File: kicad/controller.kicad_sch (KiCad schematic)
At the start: 18 parts, among them J9 SWD, SW6 RESET, U6 Pico, U7 TL431

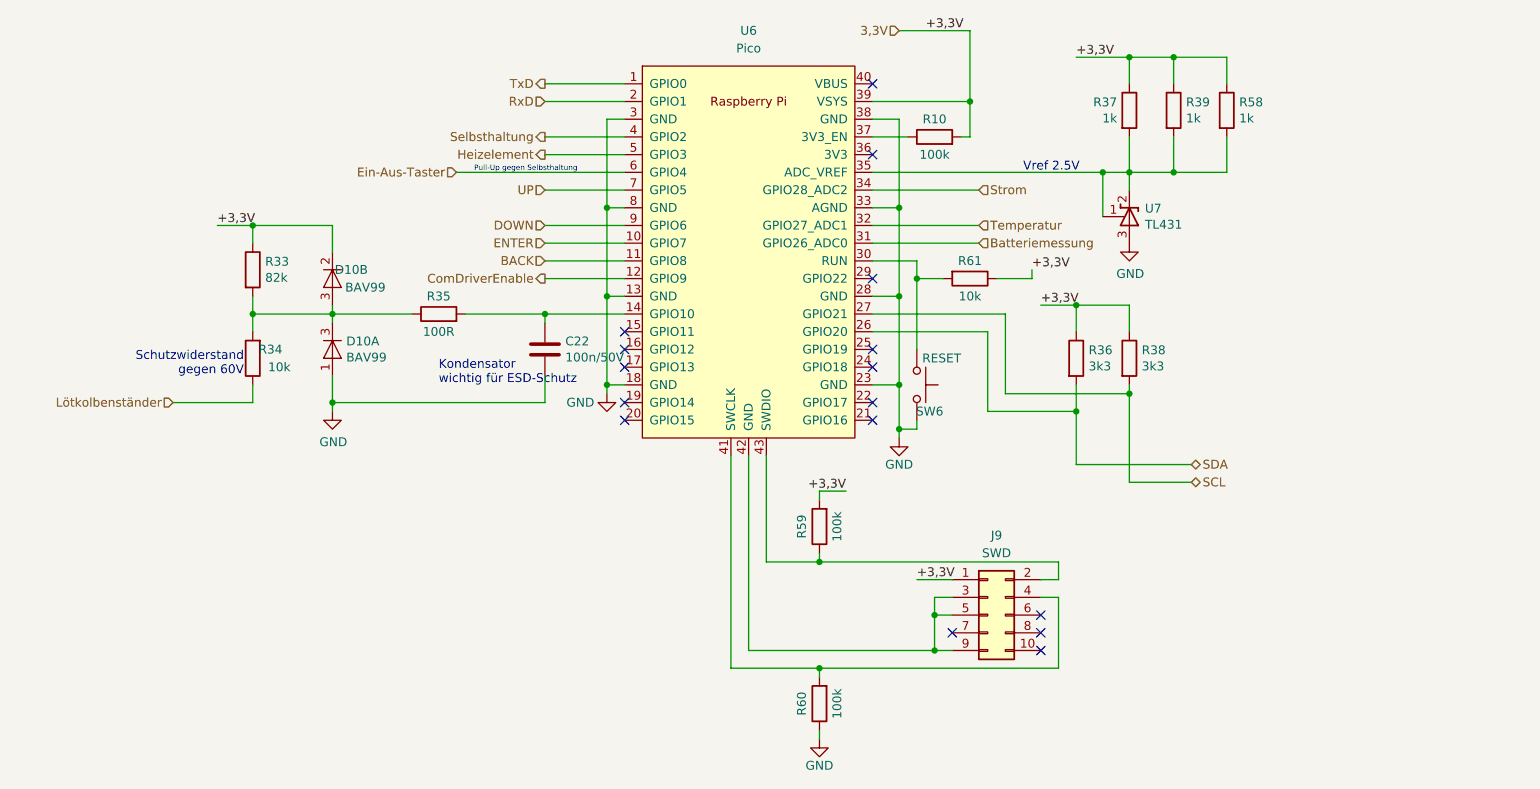
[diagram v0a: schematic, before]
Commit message: Schottky in Pico-Versorgung, VREF korrigiert auf 3.0V
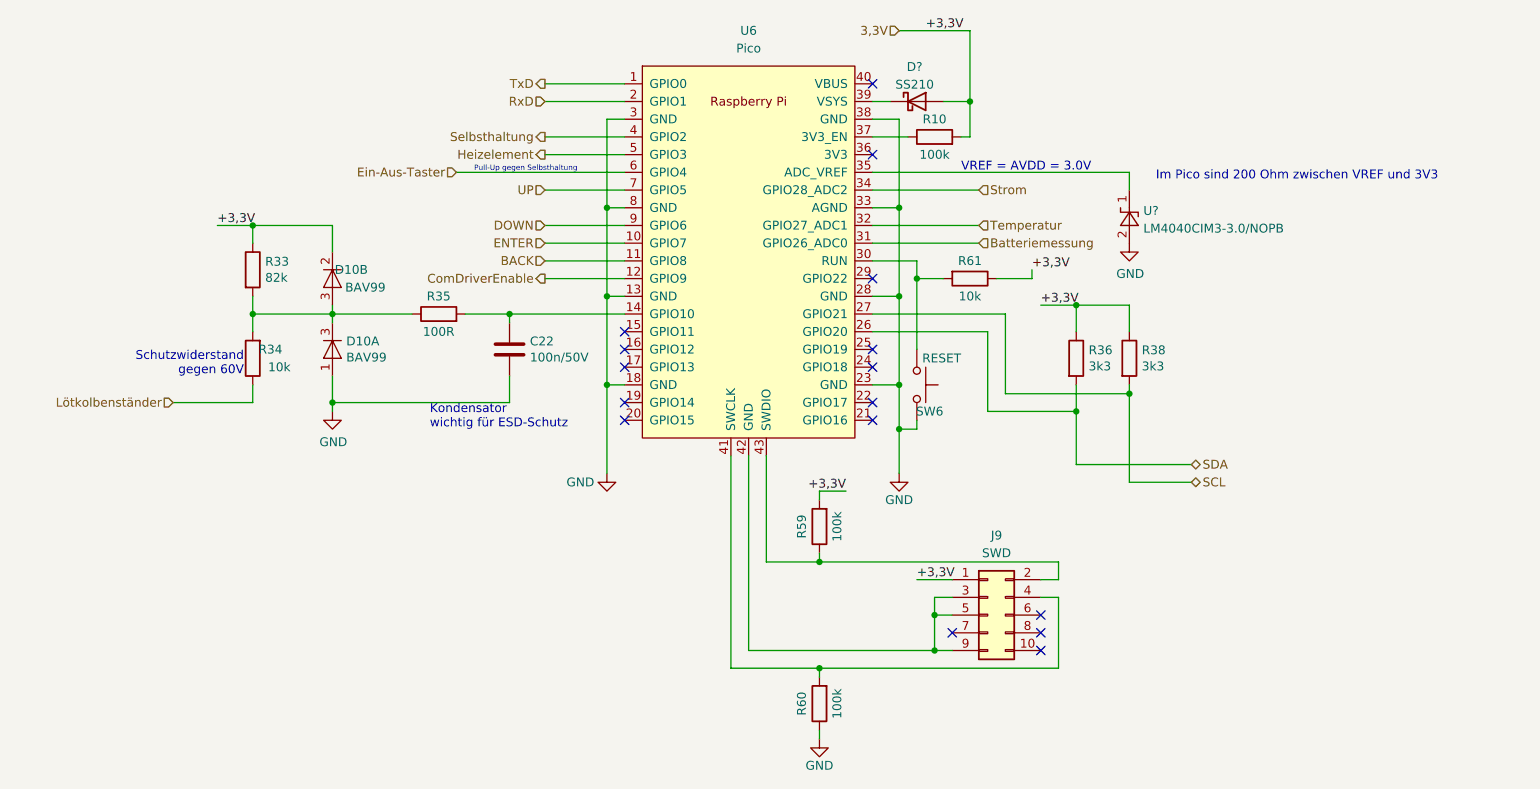
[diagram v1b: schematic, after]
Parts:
- removed R37, R39, R58: 1k, Resistor_SMD:R_1206_3216Metric, symbol Device:R
- removed U7: TL431, Package_TO_SOT_SMD:SOT-23, symbol htl_ics:TL431
- added D?: SS210, htl_smd:D_SMA_wide, symbol Device:D_Schottky
- added U?: LM4040CIM3-3.0/NOPB, Package_TO_SOT_SMD:SOT-23, symbol Reference_Voltage:LM4040DBZ-2.0
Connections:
- net 3,3V: now also D?.2 (A); no longer U6.39 (VSYS)
- net GND: now also U?.2 (A)
- net at U6.35 (ADC_VREF): now also U?.1 (K)
- new net: D?.1 (K), U6.39 (VSYS)
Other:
- note added: "Im Pico sind 200 Ohm zwischen VREF und 3V3"
- note added: "VREF = AVDD = 3.0V"
- note removed: "Vref 2.5V"
- moved on the sheet: C22

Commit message: BOM auf Lieferbarkeit aktualisiert, TODO: DRC bereinigen
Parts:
- R36, R38: DistOrderNr C229599 -> C137292
- gave numbers to parts that had none: 2
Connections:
- net 3V3_EN: now reaches R10.1, U6.37 (3V3_EN)
- net VREF: now reaches U6.35 (ADC_VREF), U7.1 (K)
- net RUN: now reaches R61.2, SW6.1, U6.30 (RUN)
- net VSYS: now reaches D15.1 (K), U6.39 (VSYS)
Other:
- moved on the sheet: D15, R10

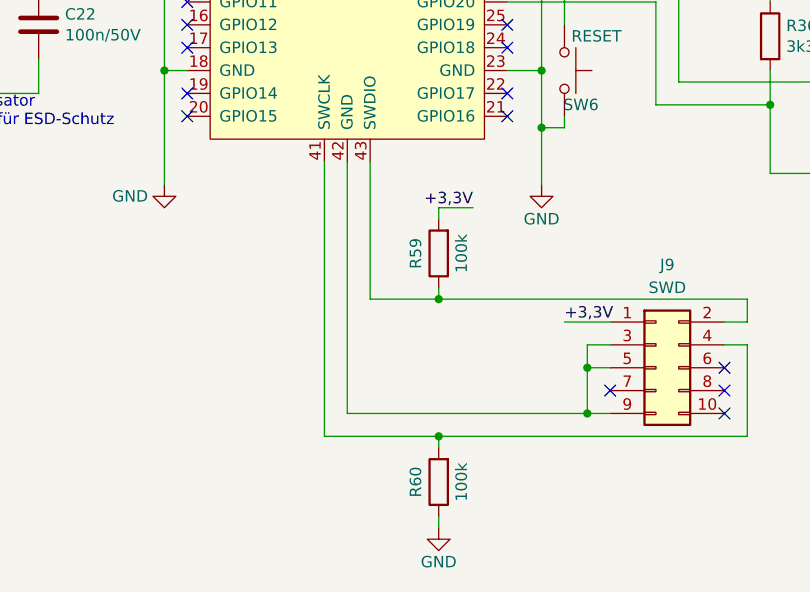
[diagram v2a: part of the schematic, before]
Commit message: PCB fertig. Platzierung verbessert (Federklemme unter OLED)
Layout minimal verbessert
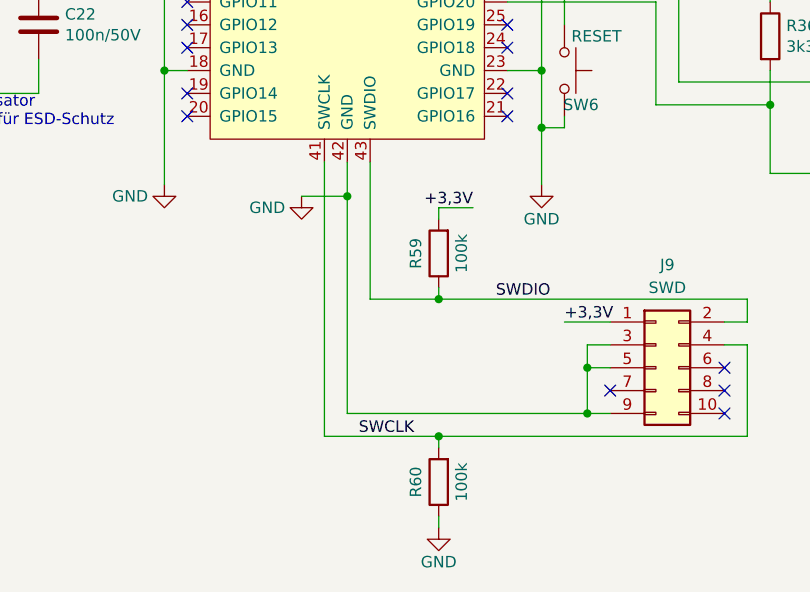
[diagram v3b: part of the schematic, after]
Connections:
- net GND: now also J9.3 (Pin_3), J9.5 (Pin_5), J9.9 (Pin_9), U6.42 (GND)
- net SWDIO: now reaches J9.2 (Pin_2), R59.1, U6.43 (SWDIO)
- net SWCLK: now reaches J9.4 (Pin_4), R60.2, U6.41 (SWCLK)
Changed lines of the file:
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@@
   (title_block
     (title "HTL Lötregler Mini")
-    (date "2023-02-15")
-    (rev "22.0.0-dev")
+    (date "2023-03-01")
+    (rev "22.0.0")
     (company "HTL Steyr")
     (comment 1 "Prof. Karl Zeilhofer et al.")
+  )
+  (junction (at 142.24 123.19) (diameter 0) (color 0 0 0 0)
   )
   (junction (at 82.55 99.06) (diameter 0) (color 0 0 0 0)
@@
     (stroke (width 0) (type default) (color 0 0 0 0))
   )
+  (wire (pts (xy 137.16 123.19) (xy 142.24 123.19))
+    (stroke (width 0) (type default) (color 0 0 0 0))
+  )
   (wire (pts (xy 166.37 93.98) (xy 166.37 104.14))
     (stroke (width 0) (type default) (color 0 0 0 0))
@@
     (stroke (width 0) (type default) (color 0 0 0 0))
   )
+  (wire (pts (xy 142.24 123.19) (xy 142.24 147.32))
+    (stroke (width 0) (type default) (color 0 0 0 0))
+  )
   (wire (pts (xy 175.26 81.28) (xy 160.02 81.28))
     (stroke (width 0) (type default) (color 0 0 0 0))
   )
-  (wire (pts (xy 142.24 119.38) (xy 142.24 147.32))
+  (wire (pts (xy 142.24 119.38) (xy 142.24 123.19))
     (stroke (width 0) (type default) (color 0 0 0 0))
   )
@@
     (effects (font (size 1.27 1.27)) (justify left bottom))
   )
+  (label "SWCLK" (at 143.51 149.86 0)
+    (effects (font (size 1.27 1.27)) (justify left bottom))
+  )
   (label "+3,3V" (at 66.04 86.36 0)
     (effects (font (size 1.27 1.27)) (justify left bottom))
@@
   )
   (label "+3,3V" (at 166.37 137.16 0)
+    (effects (font (size 1.27 1.27)) (justify left bottom))
+  )
+  (label "SWDIO" (at 158.75 134.62 0)
     (effects (font (size 1.27 1.27)) (justify left bottom))
   )
@@
     (pin "9")
   )
+  (symbol (lib_id "power:GND") (at 137.16 123.19 0) (unit 1)
+    (in_bom yes) (on_board yes)
+    (property "Reference" "#PWR0105" (id 0) (at 137.16 129.54 0)
+      (effects (font (size 1.27 1.27)) hide)
+    )
+    (property "Value" "GND" (id 1) (at 133.35 124.46 0))
+    (property "Footprint" "" (id 2) (at 137.16 123.19 0)
+      (effects (font (size 1.27 1.27)) hide)
+    )
+    (property "Datasheet" "" (id 3) (at 137.16 123.19 0)
+      (effects (font (size 1.27 1.27)) hide)
+    )
+    (pin "1")
+  )
   (symbol (lib_id "Device:R") (at 189.23 105.41 0) (unit 1)
